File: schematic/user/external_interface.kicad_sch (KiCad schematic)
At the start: 30 parts, among them J2 Radio_Jack, J3 User_Jack, Q3 MBT3904DW1T1, Q4 MBT3904DW1T1, Q5 MBT3904DW1T1, SW3 PTT_Button, SW4 Mode_Button, SW5 Vol_Up_Button, SW6 Vol_Down_Button

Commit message: v0.4 board: substitute JLCPCB basic parts where possible ($3/component savings).
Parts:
- D6: LCSC C193191 -> C72041
- R23, R28, R30, R31, R34: LCSC C269437 -> C13167
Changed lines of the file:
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@@
       (effects (font (size 1.27 1.27)) hide)
     )
-    (property "Datasheet" "https://datasheet.lcsc.com/lcsc/1811101310_TyoHM-RMC06032-7K5-N_C269437.pdf" (id 3) (at 133.35 73.66 0)
-      (effects (font (size 1.27 1.27)) hide)
-    )
-    (property "LCSC" "C269437" (id 4) (at 133.35 73.66 0)
+    (property "Datasheet" "https://datasheet.lcsc.com/lcsc/2206010216_UNI-ROYAL-Uniroyal-Elec-0603WAF2701T5E_C13167.pdf" (id 3) (at 133.35 73.66 0)
+      (effects (font (size 1.27 1.27)) hide)
+    )
+    (property "LCSC" "C13167" (id 4) (at 133.35 73.66 0)
       (effects (font (size 1.27 1.27)) hide)
     )
@@
       (effects (font (size 1.27 1.27)) hide)
     )
-    (property "Datasheet" "https://datasheet.lcsc.com/lcsc/1811100911_Orient-ORH-B36G_C193191.pdf" (id 3) (at 138.43 140.97 0)
-      (effects (font (size 1.27 1.27)) hide)
-    )
-    (property "LCSC" "C193191" (id 4) (at 138.43 140.97 0)
+    (property "Datasheet" "https://datasheet.lcsc.com/lcsc/1811101510_Everlight-Elec-19-217-BHC-ZL1M2RY-3T_C72041.pdf" (id 3) (at 138.43 140.97 0)
+      (effects (font (size 1.27 1.27)) hide)
+    )
+    (property "LCSC" "C72041" (id 4) (at 138.43 140.97 0)
       (effects (font (size 1.27 1.27)) hide)
     )
@@
       (effects (font (size 1.27 1.27)) hide)
     )
-    (property "Datasheet" "https://datasheet.lcsc.com/lcsc/1811101310_TyoHM-RMC06032-7K5-N_C269437.pdf" (id 3) (at 93.98 74.93 0)
-      (effects (font (size 1.27 1.27)) hide)
-    )
-    (property "LCSC" "C269437" (id 4) (at 93.98 74.93 0)
+    (property "Datasheet" "https://datasheet.lcsc.com/lcsc/2206010216_UNI-ROYAL-Uniroyal-Elec-0603WAF2701T5E_C13167.pdf" (id 3) (at 93.98 74.93 0)
+      (effects (font (size 1.27 1.27)) hide)
+    )
+    (property "LCSC" "C13167" (id 4) (at 93.98 74.93 0)
       (effects (font (size 1.27 1.27)) hide)
     )
@@
       (effects (font (size 1.27 1.27)) hide)
     )
-    (property "Datasheet" "https://datasheet.lcsc.com/lcsc/1811101310_TyoHM-RMC06032-7K5-N_C269437.pdf" (id 3) (at 38.1 74.93 0)
-      (effects (font (size 1.27 1.27)) hide)
-    )
-    (property "LCSC" "C269437" (id 4) (at 38.1 74.93 0)
+    (property "Datasheet" "https://datasheet.lcsc.com/lcsc/2206010216_UNI-ROYAL-Uniroyal-Elec-0603WAF2701T5E_C13167.pdf" (id 3) (at 38.1 74.93 0)
+      (effects (font (size 1.27 1.27)) hide)
+    )
+    (property "LCSC" "C13167" (id 4) (at 38.1 74.93 0)
       (effects (font (size 1.27 1.27)) hide)
     )
@@
       (effects (font (size 1.27 1.27)) hide)
     )
-    (property "Datasheet" "https://datasheet.lcsc.com/lcsc/1811101310_TyoHM-RMC06032-7K5-N_C269437.pdf" (id 3) (at 124.46 152.4 0)
-      (effects (font (size 1.27 1.27)) hide)
-    )
-    (property "LCSC" "C269437" (id 4) (at 124.46 152.4 0)
+    (property "Datasheet" "https://datasheet.lcsc.com/lcsc/2206010216_UNI-ROYAL-Uniroyal-Elec-0603WAF2701T5E_C13167.pdf" (id 3) (at 124.46 152.4 0)
+      (effects (font (size 1.27 1.27)) hide)
+    )
+    (property "LCSC" "C13167" (id 4) (at 124.46 152.4 0)
       (effects (font (size 1.27 1.27)) hide)
     )
@@
       (effects (font (size 1.27 1.27)) hide)
     )
-    (property "Datasheet" "https://datasheet.lcsc.com/lcsc/1811101310_TyoHM-RMC06032-7K5-N_C269437.pdf" (id 3) (at 176.53 73.66 0)
-      (effects (font (size 1.27 1.27)) hide)
-    )
-    (property "LCSC" "C269437" (id 4) (at 176.53 73.66 0)
-      (effects (font (size 1.27 1.27)) hide)
-    )
+    (property "Datasheet" "https://datasheet.lcsc.com/lcsc/2206010216_UNI-ROYAL-Uniroyal-Elec-0603WAF2701T5E_C13167.pdf" (id 3) (at 176.53 73.66 0)
+      (effects (font (size 1.27 1.27)) hide)
+    )
+    (property "LCSC" "C13167" (id 4) (at 176.53 73.66 0)
+      (effects (font (size 1.27 1.27)) hide)
+    )

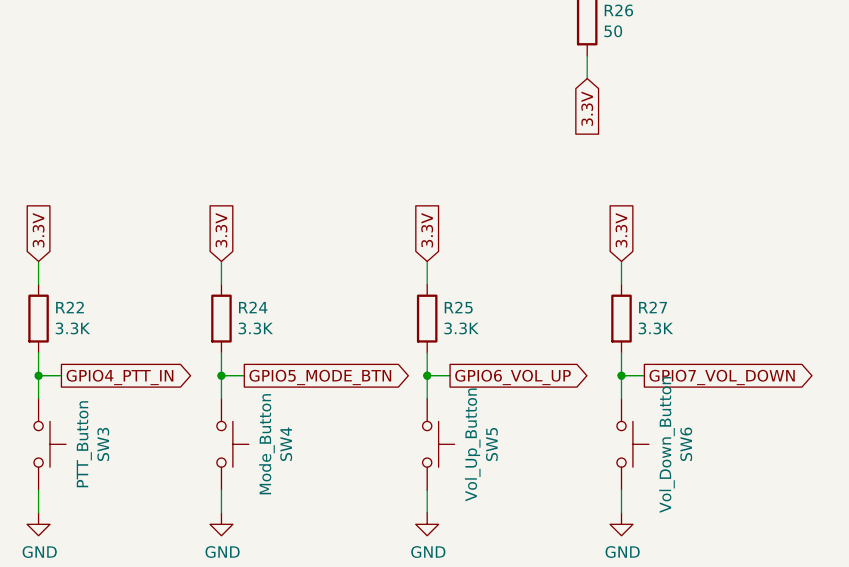
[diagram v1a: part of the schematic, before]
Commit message: v0.4 board: rm unnecesary pullups, update button/LED labeling
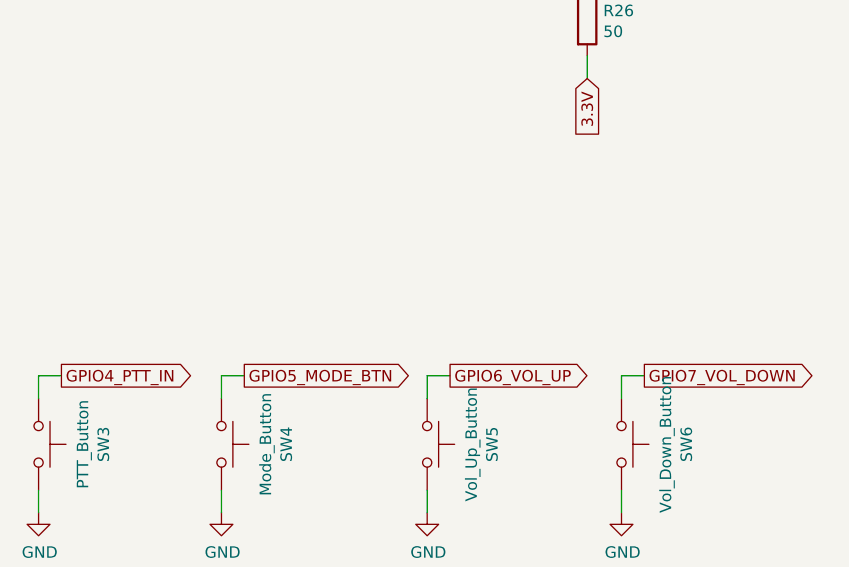
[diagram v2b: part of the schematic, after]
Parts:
- removed R22, R24, R25, R27: 3.3K, Resistor_SMD:R_0603_1608Metric, symbol Device:R
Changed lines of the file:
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@@
 (kicad_sch (version 20211123) (generator eeschema)
   (paper "A4")
-  (junction (at 43.18 142.24) (diameter 0) (color 0 0 0 0)
-  )
   (junction (at 87.63 43.18) (diameter 0) (color 0 0 0 0)
   )
-  (junction (at 22.86 142.24) (diameter 0) (color 0 0 0 0)
-  )
-  (junction (at 87.63 142.24) (diameter 0) (color 0 0 0 0)
-  )
-  (junction (at 66.04 142.24) (diameter 0) (color 0 0 0 0)
-  )
-  (wire (pts (xy 87.63 139.7) (xy 87.63 142.24))
-    (stroke (width 0) (type default) (color 0 0 0 0))
-  )
   (wire (pts (xy 133.35 77.47) (xy 133.35 80.01))
     (stroke (width 0) (type default) (color 0 0 0 0))
@@
     (stroke (width 0) (type default) (color 0 0 0 0))
   )
-  (wire (pts (xy 66.04 139.7) (xy 66.04 142.24))
-    (stroke (width 0) (type default) (color 0 0 0 0))
-  )
   (wire (pts (xy 85.09 39.37) (xy 90.17 39.37))
     (stroke (width 0) (type default) (color 0 0 0 0))
@@
     (stroke (width 0) (type default) (color 0 0 0 0))
   )
-  (wire (pts (xy 43.18 139.7) (xy 43.18 142.24))
-    (stroke (width 0) (type default) (color 0 0 0 0))
-  )
   (wire (pts (xy 123.19 97.79) (xy 123.19 95.25))
     (stroke (width 0) (type default) (color 0 0 0 0))
@@
     (stroke (width 0) (type default) (color 0 0 0 0))
   )
-  (wire (pts (xy 22.86 139.7) (xy 22.86 142.24))
-    (stroke (width 0) (type default) (color 0 0 0 0))
-  )
   (wire (pts (xy 172.72 73.66) (xy 170.18 73.66))
     (stroke (width 0) (type default) (color 0 0 0 0))
   )
-  (wire (pts (xy 43.18 129.54) (xy 43.18 132.08))
-    (stroke (width 0) (type default) (color 0 0 0 0))
-  )
   (wire (pts (xy 83.82 76.2) (xy 83.82 73.66))
     (stroke (width 0) (type default) (color 0 0 0 0))
@@
     (stroke (width 0) (type default) (color 0 0 0 0))
   )
-  (wire (pts (xy 87.63 129.54) (xy 87.63 132.08))
-    (stroke (width 0) (type default) (color 0 0 0 0))
-  )
   (wire (pts (xy 118.11 152.4) (xy 118.11 149.86))
     (stroke (width 0) (type default) (color 0 0 0 0))
@@
     (stroke (width 0) (type default) (color 0 0 0 0))
   )
-  (wire (pts (xy 66.04 129.54) (xy 66.04 132.08))
-    (stroke (width 0) (type default) (color 0 0 0 0))
-  )
   (wire (pts (xy 45.72 142.24) (xy 43.18 142.24))
     (stroke (width 0) (type default) (color 0 0 0 0))
@@
     (stroke (width 0) (type default) (color 0 0 0 0))
   )
-  (wire (pts (xy 22.86 129.54) (xy 22.86 132.08))
-    (stroke (width 0) (type default) (color 0 0 0 0))
-  )
   (wire (pts (xy 87.63 142.24) (xy 87.63 144.78))
     (stroke (width 0) (type default) (color 0 0 0 0))
@@
     )
   )
-  (global_label "3.3V" (shape input) (at 43.18 129.54 90) (fields_autoplaced)
-    (effects (font (size 1.27 1.27)) (justify left))
-    (property "Intersheet References" "${INTERSHEET_REFS}" (id 0) (at -2.54 10.16 0)
-      (effects (font (size 1.27 1.27)) hide)
-    )
-  )
   (global_label "GPIO5_MODE_BTN" (shape output) (at 45.72 142.24 0) (fields_autoplaced)
     (effects (font (size 1.27 1.27)) (justify left))
@@
   )
   (global_label "GPIO6_VOL_UP" (shape output) (at 68.58 142.24 0) (fields_autoplaced)
-    (effects (font (size 1.27 1.27)) (justify left))
-    (property "Intersheet References" "${INTERSHEET_REFS}" (id 0) (at -2.54 10.16 0)
-      (effects (font (size 1.27 1.27)) hide)
-    )
-  )
-  (global_label "3.3V" (shape input) (at 66.04 129.54 90) (fields_autoplaced)
     (effects (font (size 1.27 1.27)) (justify left))
     (property "Intersheet References" "${INTERSHEET_REFS}" (id 0) (at -2.54 10.16 0)
@@
     )
   )
-  (global_label "3.3V" (shape input) (at 87.63 129.54 90) (fields_autoplaced)
-    (effects (font (size 1.27 1.27)) (justify left))
-    (property "Intersheet References" "${INTERSHEET_REFS}" (id 0) (at -2.54 10.16 0)
-      (effects (font (size 1.27 1.27)) hide)
-    )
-  )
   (global_label "GPIO4_PTT_IN" (shape output) (at 25.4 142.24 0) (fields_autoplaced)
     (effects (font (size 1.27 1.27)) (justify left))
@@
     (effects (font (size 1.27 1.27)) (justify left))
     (property "Intersheet References" "${INTERSHEET_REFS}" (id 0) (at -2.54 11.43 0)
-      (effects (font (size 1.27 1.27)) hide)
-    )
-  )
-  (global_label "3.3V" (shape input) (at 22.86 129.54 90) (fields_autoplaced)
-    (effects (font (size 1.27 1.27)) (justify left))
-    (property "Intersheet References" "${INTERSHEET_REFS}" (id 0) (at -2.54 10.16 0)
       (effects (font (size 1.27 1.27)) hide)
     )
@@
     (pin "2")
   )
-  (symbol (lib_id "Device:R") (at 43.18 135.89 0) (unit 1)
-    (in_bom yes) (on_board yes)
-    (property "Reference" "R24" (id 0) (at 44.958 134.7216 0)
-      (effects (font (size 1.27 1.27)) (justify left))
-    )
-    (property "Value" "3.3K" (id 1) (at 44.958 137.033 0)
-      (effects (font (size 1.27 1.27)) (justify left))
-    )
-    (property "Footprint" "Resistor_SMD:R_0603_1608Metric" (id 2) (at 41.402 135.89 90)
-      (effects (font (size 1.27 1.27)) hide)
-    )
-    (property "Datasheet" "https://datasheet.lcsc.com/lcsc/2110252130_UNI-ROYAL-Uniroyal-Elec-0603WAF3301T5E_C22978.pdf" (id 3) (at 43.18 135.89 0)
-      (effects (font (size 1.27 1.27)) hide)
-    )
-    (property "LCSC" "C22978" (id 4) (at 43.18 135.89 0)
-      (effects (font (size 1.27 1.27)) hide)
-    )
-    (pin "1")
-    (pin "2")
-  )
   (symbol (lib_id "Device:LED") (at 123.19 91.44 270) (unit 1)
     (in_bom yes) (on_board yes)
@@
     (pin "1")
   )
-  (symbol (lib_id "Device:R") (at 87.63 135.89 0) (unit 1)
-    (in_bom yes) (on_board yes)
-    (property "Reference" "R27" (id 0) (at 89.408 134.7216 0)
-      (effects (font (size 1.27 1.27)) (justify left))
-    )
-    (property "Value" "3.3K" (id 1) (at 89.408 137.033 0)
-      (effects (font (size 1.27 1.27)) (justify left))
-    )
-    (property "Footprint" "Resistor_SMD:R_0603_1608Metric" (id 2) (at 85.852 135.89 90)
-      (effects (font (size 1.27 1.27)) hide)
-    )
-    (property "Datasheet" "https://datasheet.lcsc.com/lcsc/2110252130_UNI-ROYAL-Uniroyal-Elec-0603WAF3301T5E_C22978.pdf" (id 3) (at 87.63 135.89 0)
-      (effects (font (size 1.27 1.27)) hide)
-    )
-    (property "LCSC" "C22978" (id 4) (at 87.63 135.89 0)
-      (effects (font (size 1.27 1.27)) hide)
-    )
-    (pin "1")
-    (pin "2")
-  )
-  (symbol (lib_id "Device:R") (at 66.04 135.89 0) (unit 1)
-    (in_bom yes) (on_board yes)
-    (property "Reference" "R25" (id 0) (at 67.818 134.7216 0)
-      (effects (font (size 1.27 1.27)) (justify left))
-    )
-    (property "Value" "3.3K" (id 1) (at 67.818 137.033 0)
-      (effects (font (size 1.27 1.27)) (justify left))
-    )
-    (property "Footprint" "Resistor_SMD:R_0603_1608Metric" (id 2) (at 64.262 135.89 90)
-      (effects (font (size 1.27 1.27)) hide)
-    )
-    (property "Datasheet" "https://datasheet.lcsc.com/lcsc/2110252130_UNI-ROYAL-Uniroyal-Elec-0603WAF3301T5E_C22978.pdf" (id 3) (at 66.04 135.89 0)
-      (effects (font (size 1.27 1.27)) hide)
-    )
-    (property "LCSC" "C22978" (id 4) (at 66.04 135.89 0)
-      (effects (font (size 1.27 1.27)) hide)
-    )
-    (pin "1")
-    (pin "2")
-  )
   (symbol (lib_id "power:GND") (at 83.82 73.66 180) (unit 1)
     (in_bom yes) (on_board yes)
@@
     (pin "1")
   )
-  (symbol (lib_id "Device:R") (at 22.86 135.89 0) (unit 1)
-    (in_bom yes) (on_board yes)
-    (property "Reference" "R22" (id 0) (at 24.638 134.7216 0)
-      (effects (font (size 1.27 1.27)) (justify left))
-    )
-    (property "Value" "3.3K" (id 1) (at 24.638 137.033 0)
-      (effects (font (size 1.27 1.27)) (justify left))
-    )
-    (property "Footprint" "Resistor_SMD:R_0603_1608Metric" (id 2) (at 21.082 135.89 90)
-      (effects (font (size 1.27 1.27)) hide)
-    )
-    (property "Datasheet" "https://datasheet.lcsc.com/lcsc/2110252130_UNI-ROYAL-Uniroyal-Elec-0603WAF3301T5E_C22978.pdf" (id 3) (at 22.86 135.89 0)
-      (effects (font (size 1.27 1.27)) hide)
-    )
-    (property "LCSC" "C22978" (id 4) (at 22.86 135.89 0)
-      (effects (font (size 1.27 1.27)) hide)
-    )
-    (pin "1")
-    (pin "2")
-  )
   (symbol (lib_id "Switch:SW_Push") (at 87.63 149.86 270) (unit 1)

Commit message: v0.4 board submitted for build/assembly.
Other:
- company: (none) -> FreeDV Project
- title: (none) -> ezDV External Interface
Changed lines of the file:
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@@
 (kicad_sch (version 20211123) (generator eeschema)
   (paper "A4")
+  (title_block
+    (title "ezDV External Interface")
+    (date "2022-10-01")
+    (rev "v0.4")
+    (company "FreeDV Project")
+  )
   (junction (at 87.63 43.18) (diameter 0) (color 0 0 0 0)
   )

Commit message: v0.5 board: move PERIPH_PWR GPIO to RTC to make sure it stays off when sleeping.
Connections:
- net 3.3V renamed 3.3V_PERIPH
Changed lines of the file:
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@@
     )
   )
-  (global_label "3.3V" (shape output) (at 140.97 127 0) (fields_autoplaced)
+  (global_label "3.3V_PERIPH" (shape output) (at 140.97 127 0) (fields_autoplaced)
     (effects (font (size 1.27 1.27)) (justify left))
-    (property "Intersheet References" "${INTERSHEET_REFS}" (id 0) (at 3.81 22.86 0)
-      (effects (font (size 1.27 1.27)) hide)
+    (property "Intersheet References" "${INTERSHEET_REFS}" (id 0) (at 155.3574 126.9206 0)
+      (effects (font (size 1.27 1.27)) (justify left) hide)
     )
   )
@@
     )
   )
-  (global_label "3.3V" (shape input) (at 83.82 109.22 270) (fields_autoplaced)
+  (global_label "3.3V_PERIPH" (shape input) (at 83.82 109.22 270) (fields_autoplaced)
     (effects (font (size 1.27 1.27)) (justify right))
-    (property "Intersheet References" "${INTERSHEET_REFS}" (id 0) (at -2.54 10.16 0)
-      (effects (font (size 1.27 1.27)) hide)
+    (property "Intersheet References" "${INTERSHEET_REFS}" (id 0) (at 83.7406 123.6074 90)
+      (effects (font (size 1.27 1.27)) (justify right) hide)
     )
   )
@@
     )
   )
-  (global_label "3.3V" (shape input) (at 123.19 107.95 270) (fields_autoplaced)
+  (global_label "3.3V_PERIPH" (shape input) (at 123.19 107.95 270) (fields_autoplaced)
     (effects (font (size 1.27 1.27)) (justify right))
-    (property "Intersheet References" "${INTERSHEET_REFS}" (id 0) (at -2.54 10.16 0)
-      (effects (font (size 1.27 1.27)) hide)
+    (property "Intersheet References" "${INTERSHEET_REFS}" (id 0) (at 123.1106 122.3374 90)
+      (effects (font (size 1.27 1.27)) (justify right) hide)
     )
   )
@@
     )
   )
-  (global_label "3.3V" (shape input) (at 162.56 101.6 270) (fields_autoplaced)
+  (global_label "3.3V_PERIPH" (shape input) (at 162.56 101.6 270) (fields_autoplaced)
     (effects (font (size 1.27 1.27)) (justify right))
-    (property "Intersheet References" "${INTERSHEET_REFS}" (id 0) (at -2.54 10.16 0)
-      (effects (font (size 1.27 1.27)) hide)
+    (property "Intersheet References" "${INTERSHEET_REFS}" (id 0) (at 162.4806 115.9874 90)
+      (effects (font (size 1.27 1.27)) (justify right) hide)
     )
   )

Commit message: v0.5 board: Add PTT input breakout.
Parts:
- added J5: PTT Breakout, Connector_PinHeader_2.54mm:PinHeader_1x02_P2.54mm_Vertical, symbol Connector:Conn_01x02_Female
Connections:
- net GND: now also J5.1 (Pin_1)
- net GPIO4_PTT_IN: now also J5.2 (Pin_2)
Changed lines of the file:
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@@
   (junction (at 87.63 43.18) (diameter 0) (color 0 0 0 0)
   )
+  (junction (at 22.86 142.24) (diameter 0) (color 0 0 0 0)
+  )
   (wire (pts (xy 133.35 77.47) (xy 133.35 80.01))
     (stroke (width 0) (type default) (color 0 0 0 0))
@@
     (stroke (width 0) (type default) (color 0 0 0 0))
   )
+  (wire (pts (xy 22.86 132.08) (xy 22.86 142.24))
+    (stroke (width 0) (type default) (color 0 0 0 0))
+  )
   (wire (pts (xy 40.64 81.28) (xy 38.1 81.28))
     (stroke (width 0) (type default) (color 0 0 0 0))
@@
     (stroke (width 0) (type default) (color 0 0 0 0))
   )
+  (wire (pts (xy 22.86 129.54) (xy 26.67 129.54))
+    (stroke (width 0) (type default) (color 0 0 0 0))
+  )
   (wire (pts (xy 36.83 39.37) (xy 39.37 39.37))
     (stroke (width 0) (type default) (color 0 0 0 0))
@@
     (stroke (width 0) (type default) (color 0 0 0 0))
   )
+  (wire (pts (xy 22.86 125.73) (xy 22.86 129.54))
+    (stroke (width 0) (type default) (color 0 0 0 0))
+  )
   (wire (pts (xy 83.82 99.06) (xy 83.82 96.52))
     (stroke (width 0) (type default) (color 0 0 0 0))
@@
   )
   (wire (pts (xy 68.58 142.24) (xy 66.04 142.24))
+    (stroke (width 0) (type default) (color 0 0 0 0))
+  )
+  (wire (pts (xy 26.67 132.08) (xy 22.86 132.08))
     (stroke (width 0) (type default) (color 0 0 0 0))
   )
@@
     (pin "2")
   )
+  (symbol (lib_id "power:GND") (at 22.86 125.73 180) (unit 1)
+    (in_bom yes) (on_board yes) (fields_autoplaced)
+    (property "Reference" "#PWR043" (id 0) (at 22.86 119.38 0)
+      (effects (font (size 1.27 1.27)) hide)
+    )
+    (property "Value" "GND" (id 1) (at 22.86 120.65 0))
+    (property "Footprint" "" (id 2) (at 22.86 125.73 0)
+      (effects (font (size 1.27 1.27)) hide)
+    )
+    (property "Datasheet" "" (id 3) (at 22.86 125.73 0)
+      (effects (font (size 1.27 1.27)) hide)
+    )
+    (pin "1")
+  )
   (symbol (lib_id "Device:LED") (at 123.19 91.44 270) (unit 1)
     (in_bom yes) (on_board yes)
@@
     (pin "5")
   )
+  (symbol (lib_id "Connector:Conn_01x02_Female") (at 31.75 129.54 0) (unit 1)
+    (in_bom yes) (on_board yes) (fields_autoplaced)
+    (property "Reference" "J5" (id 0) (at 33.02 129.5399 0)
+      (effects (font (size 1.27 1.27)) (justify left))
+    )
+    (property "Value" "PTT Breakout" (id 1) (at 33.02 132.0799 0)
+      (effects (font (size 1.27 1.27)) (justify left))
+    )
+    (property "Footprint" "Connector_PinHeader_2.54mm:PinHeader_1x02_P2.54mm_Vertical" (id 2) (at 31.75 129.54 0)
+      (effects (font (size 1.27 1.27)) hide)
+    )
+    (property "Datasheet" "~" (id 3) (at 31.75 129.54 0)
+      (effects (font (size 1.27 1.27)) hide)
+    )
+    (pin "1")
+    (pin "2")
+  )
   (symbol (lib_id "power:GND") (at 261.62 120.65 0) (unit 1)

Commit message: v0.5 board: move PTT and NET GPIOs to RTC domain.
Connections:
- net GPIO41_PTT_LED renamed GPIO15_PTT_LED
- net GPIO42_NET_LED renamed GPIO16_NET_LED
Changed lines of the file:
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@@
     )
   )
-  (global_label "GPIO42_NET_LED" (shape output) (at 118.11 149.86 90) (fields_autoplaced)
+  (global_label "GPIO16_NET_LED" (shape output) (at 118.11 149.86 90) (fields_autoplaced)
     (effects (font (size 1.27 1.27)) (justify left))
     (property "Intersheet References" "${INTERSHEET_REFS}" (id 0) (at 3.81 22.86 0)
@@
     )
   )
-  (global_label "GPIO41_PTT_LED" (shape output) (at 182.88 71.12 90) (fields_autoplaced)
+  (global_label "GPIO15_PTT_LED" (shape output) (at 182.88 71.12 90) (fields_autoplaced)
     (effects (font (size 1.27 1.27)) (justify left))
     (property "Intersheet References" "${INTERSHEET_REFS}" (id 0) (at -2.54 10.16 0)
